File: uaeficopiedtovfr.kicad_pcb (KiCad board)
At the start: 2 copper layers, 160 x 75 mm, 68 parts, among them J1 DTF13-12PB, J4 DTF13-12PB, J9 USB_C_Receptacle_USB2.0, M1 Module-power_12and5V-0.2, M2 Module-knock-0.2, M3 Module-vr-discrete-0.4, M4 Module-vr-max9924-0.1, M5 Module-wbo-0.5, M6 Module:mega-mcu100/0.2, M7 Module-wbo-0.5, P3 Pad, P4 Pad, Q1 ISL9V3040D3S, Q10 ZXMS6005SGTA, Q11 AO3400A, Q12 AO3400A, Q13 ZXMS6005SGTA, Q14 ZXMS6005SGTA, Q15 ZXMS6005SGTA, Q16 ZXMS6005SGTA, Q2 ISL9V3040D3S, Q3 ISL9V3040D3S, Q4 ISL9V3040D3S, Q7 ZXMS6005SGTA, Q8 ZXMS6005SGTA, Q9 ZXMS6005SGTA, U2 JDY-33

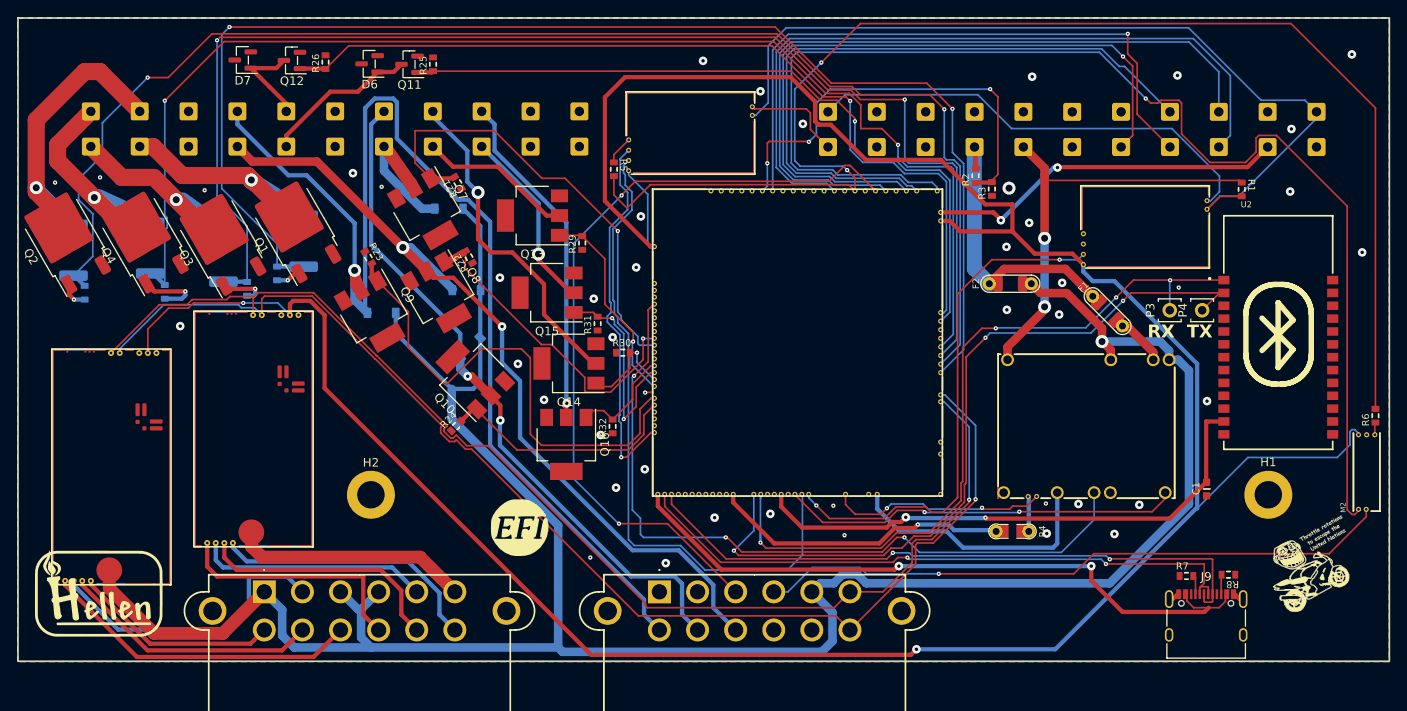
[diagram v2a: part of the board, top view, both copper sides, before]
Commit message: generate 4 layer board
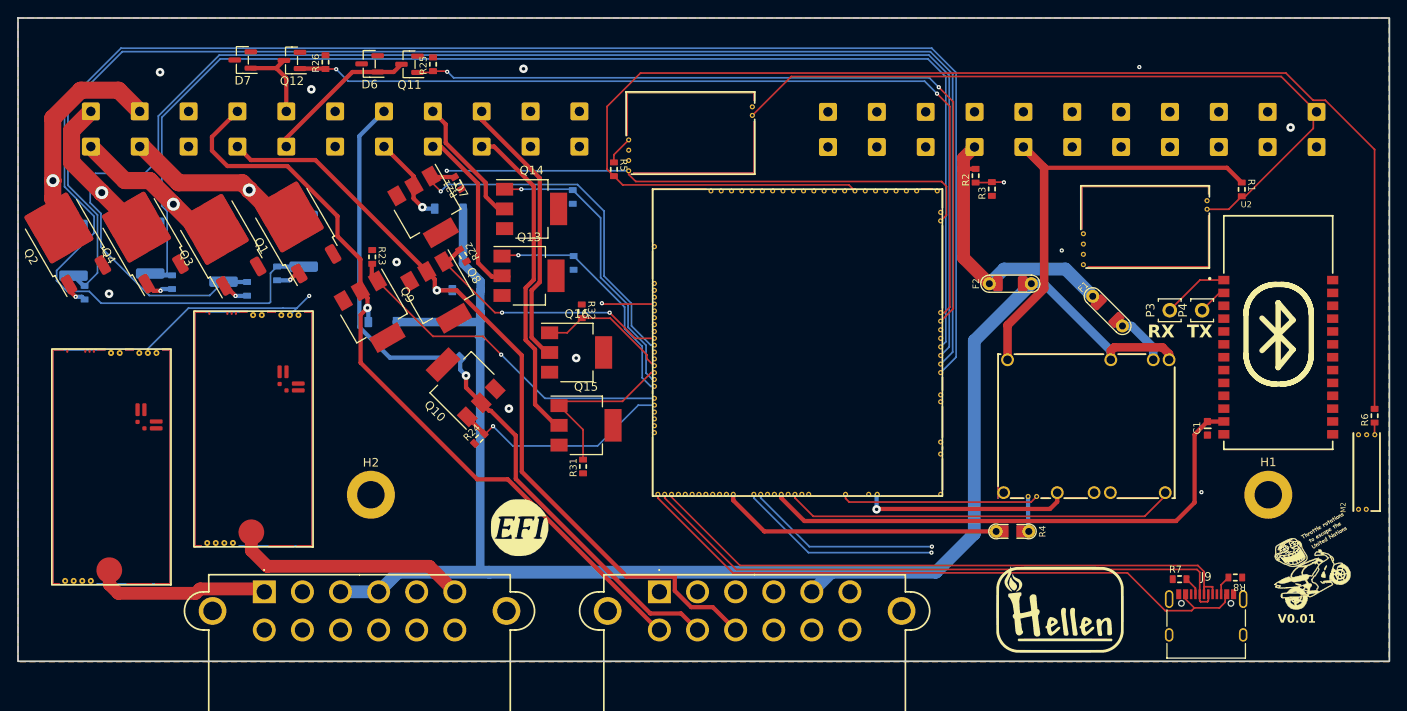
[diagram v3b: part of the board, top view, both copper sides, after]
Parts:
- R29, R30: moved to B.Cu
- moved G4 112.2 mm to (123.7, 70.5)
- moved R30 19.1 mm to (66.5, 22.2), turned to 90 degrees
- moved Q14 18.5 mm to (61.8, 23.6), turned to 0 degrees
- moved R31 16.8 mm to (67.8, 53.7)
- moved Q15 16.1 mm to (68.1, 48.9), turned to 0 degrees
- moved R32 13.9 mm to (67.6, 35.6), turned to -90 degrees
- moved Q16 10.8 mm to (67.0, 40.4), turned to 0 degrees
- moved C1 7.08 mm to (140.6, 49.2)
- moved Q13 7.04 mm to (61.5, 31.4), turned to 0 degrees
- moved R24 3.08 mm to (55.6, 50.5)
- moved R29 2.53 mm to (66.7, 29.9)
- moved Q10 1.44 mm to (53.6, 44.0)
- moved R15 1.41 mm to (19.8, 32.2)
- moved D4 1.08 mm to (44.3, 36.9)
- moved R7 0.88 mm to (137.3, 66.8)
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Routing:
- net +5VA: track 325.5 -> 188.9 mm, vias 2 -> 3
- net /VREF1: track 146.8 -> 77.8 mm
- net +12V_RAW: track 252.3 -> 189.7 mm, vias 1 -> 0
- net /IAT_SENSOR: track 80.7 -> 28.3 mm, vias 1 -> 0
- net /IGN1: track 154.9 -> 201.1 mm, vias 2 -> 0
- net /OUT_LS3: track 138.1 -> 92.0 mm
- net /CLT: track 77.1 -> 34.1 mm
- net /IN_FLEX: track 92.3 -> 129.6 mm, vias 2 -> 0
- net /IN_TPS1: track 84.6 -> 49.6 mm
- net /INJOUT2: track 39.1 -> 15.7 mm, vias 1 -> 0
- net /INJ2: track 11.4 -> 34.2 mm
- net /IGN3: track 151.9 -> 171.8 mm, vias 2 -> 0
- net /IN_MAP: track 85.7 -> 66.0 mm
- net /IN_VMAIN: track 50.1 -> 32.8 mm, vias 3 -> 1
- net /LS3: track 57.5 -> 40.5 mm, vias 0 -> 1
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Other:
- copper layers 2 -> 4
- board text added: "V0.01"

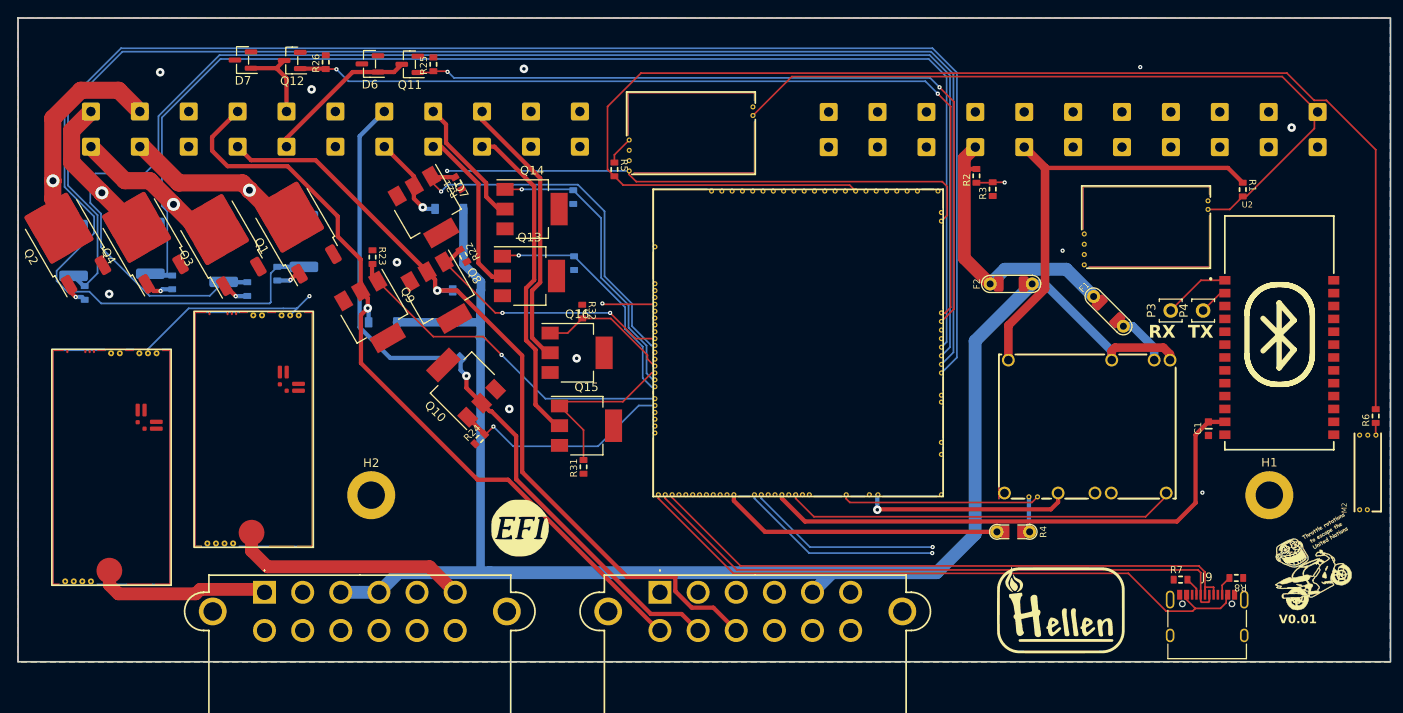
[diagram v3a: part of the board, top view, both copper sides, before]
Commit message: Added SD card support, cleaned up ignition traces
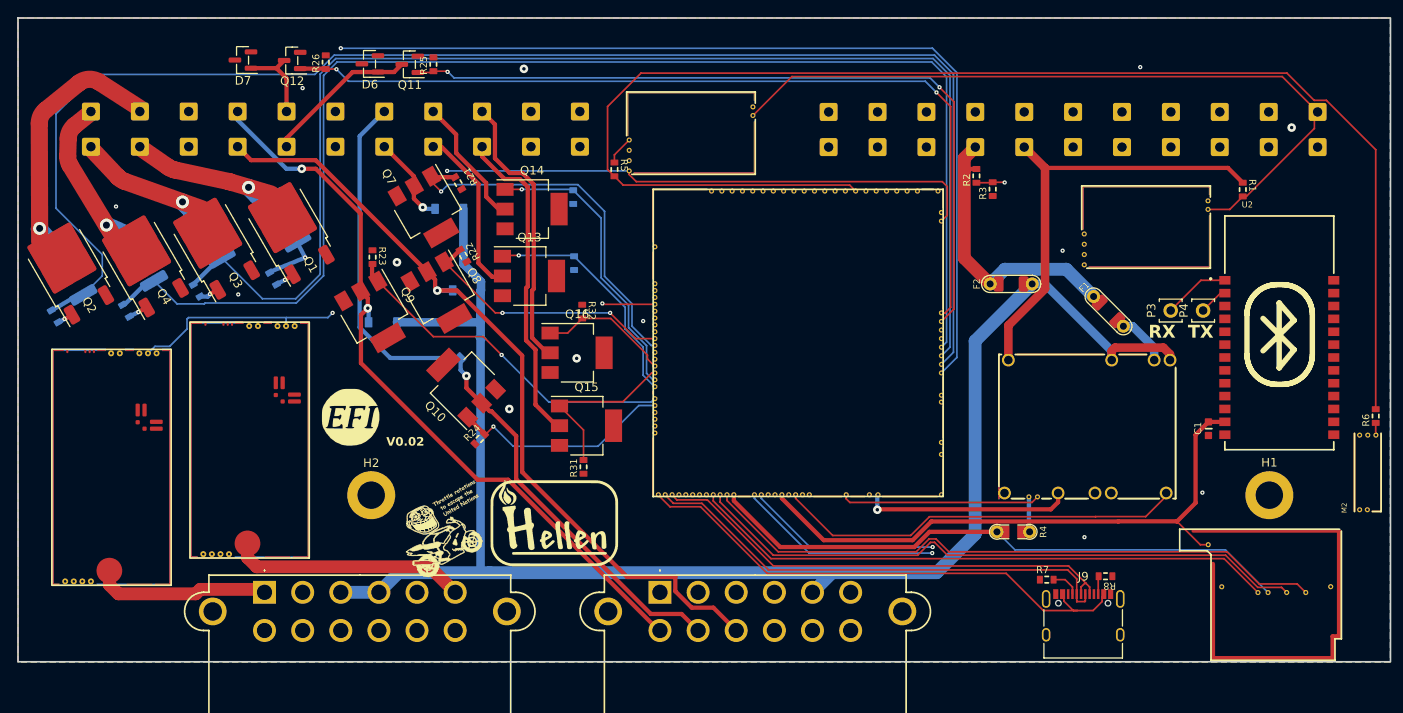
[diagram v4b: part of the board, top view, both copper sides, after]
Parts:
- added M8: Module-sd-0.1, hellen-one-sd-0.1:sd, F.Cu at (137.1, 76.3)
- moved text1 101.4 mm to (46.7, 66.5)
- moved G4 59.9 mm to (64.7, 60.4)
- moved G3 23.6 mm to (40.6, 48.0)
- moved R7 15.6 mm to (121.8, 66.8)
- moved R8 15.3 mm to (128.6, 66.5)
- moved J9 14.5 mm to (126.0, 72.2)
- moved R15 6.33 mm to (14.4, 35.5), turned to 120 degrees
- moved R11 5.90 mm to (22.6, 33.1), turned to 120 degrees
- moved R10 4.44 mm to (6.10, 36.1), turned to 120 degrees
- moved Q2 3.50 mm to (7.57, 30.5)
- moved R12 3.40 mm to (32.9, 24.9), turned to 120 degrees
- moved R14 2.96 mm to (24.1, 26.8), turned to 120 degrees
- moved Q4 2.75 mm to (16.3, 29.6)
- moved R13 2.64 mm to (7.94, 31.1), turned to 120 degrees
- moved R18 1.61 mm to (16.2, 29.4), turned to 120 degrees
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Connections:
- M6 pad N10: unconnected-(M6-SPI3_SCK_(PC10)-PadN10) -> Net-(M6-SPI3_SCK_(PC10))
- M6 pad N11: unconnected-(M6-SPI3_MISO_(PC11)-PadN11) -> Net-(M6-SPI3_MISO_(PC11))
- M6 pad N9: unconnected-(M6-SPI3_CS_(PA15)-PadN9) -> Net-(M6-SPI3_CS_(PA15))
- U1 pad B17: /VSS -> /IN_HALL1
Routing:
- net Net-(M6-SPI3_MISO_(PC11)): track 0.00 -> 73.8 mm
- net Net-(M6-SPI3_SCK_(PC10)): track 0.00 -> 72.5 mm
- net Net-(M6-SPI3_CS_(PA15)): track 0.00 -> 68.6 mm
- net /IGN1: track 201.1 -> 141.4 mm, vias 0 -> 2
- net /IN_HALL1: track 0.00 -> 42.8 mm
- net /PG_5VP: track 32.9 -> 68.9 mm
- net /IGN3: track 171.8 -> 149.1 mm
- net /USB+: track 71.4 -> 55.6 mm
- net /USB-: track 71.6 -> 56.5 mm
- net /VBUS: track 75.5 -> 61.7 mm
- net /IGNOUT3: track 25.5 -> 16.8 mm
- net /IGNOUT1: track 26.0 -> 19.2 mm
- net +3.3VA: track 62.6 -> 69.2 mm
- net /IGN4: track 150.0 -> 156.0 mm
- net /IGNOUT4: track 24.7 -> 19.9 mm
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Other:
- board text added: "V0.02"
- board text removed: "V0.01"

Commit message: adding jlcpcb order number to silkscreen
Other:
- board text added: "JLCJLCJLCJLC"
- board text added: "JLCPCB Order no:"
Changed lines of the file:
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@@
     )
+  )
+  (gr_text "JLCPCB Order no:" (at 141.1 5.5) (layer "B.SilkS")
+    (effects (font (size 1 1) (thickness 0.15)) (justify left bottom mirror))
+  )
+  (gr_text "JLCJLCJLCJLC\n" (at 127.35 5.45) (layer "B.SilkS")
+    (effects (font (size 1 1) (thickness 0.15)) (justify left bottom mirror))
   )
   (gr_text "RX  TX\n" (at 133.6 38.825) (layer "F.SilkS")
